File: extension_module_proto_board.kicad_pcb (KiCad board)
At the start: 2 copper layers, 32 parts, among them IC7 ATMEG328PU, P1 CONN_10, P10 CONN_40, P11 CONN_40, P12 CONN_40, P13 CONN_40, P14 CONN_40, P15 CONN_4, P16 CONN_6, P2 CONN_8, P3 CONN_6, P4 CONN_6, P5 CONN_40, P6 CONN_40, P7 CONN_40, P8 CONN_40, P9 CONN_40, SW1 DPST, U1 RBBB, X1 16MHz

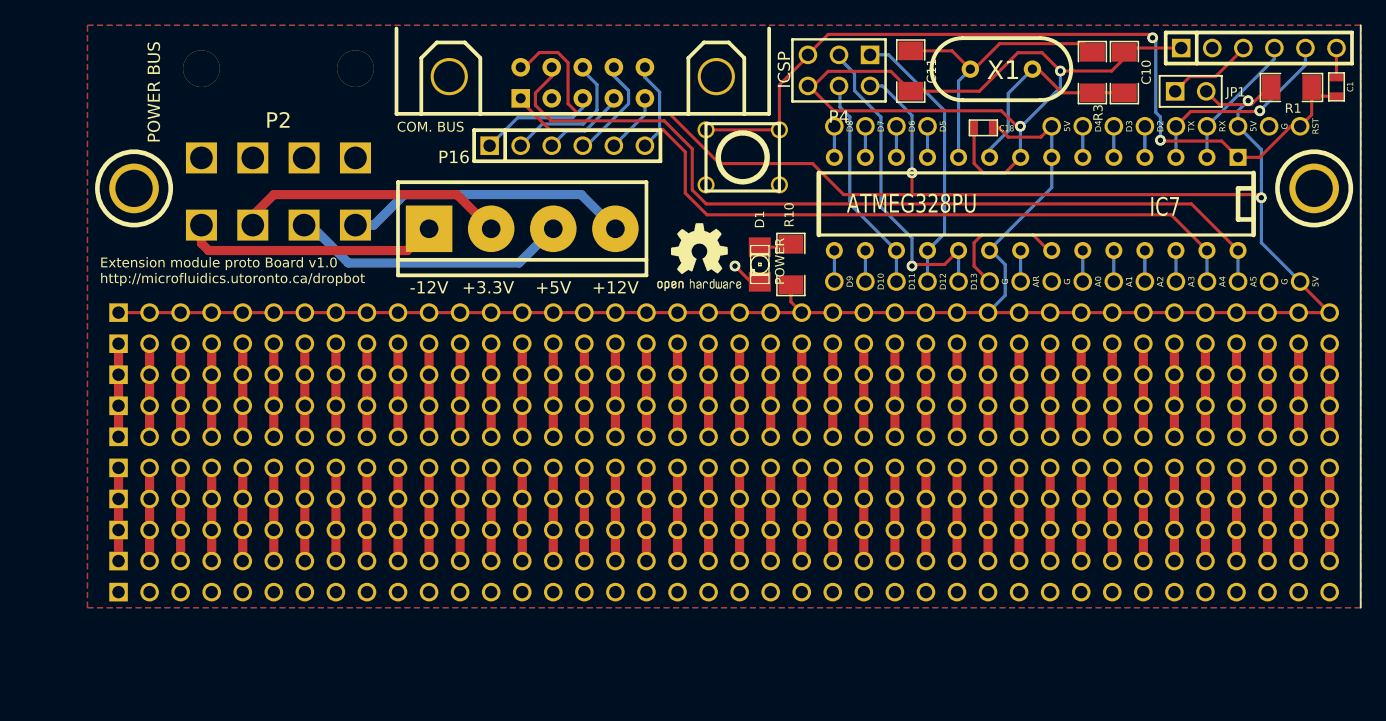
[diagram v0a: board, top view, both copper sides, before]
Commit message: Add ISP programming latch and other changes
* change layout to make board smaller
* replace 0603 caps with 1206 versions
* label VCC and GND rails
* add GND and VCC rail on either side of proto area
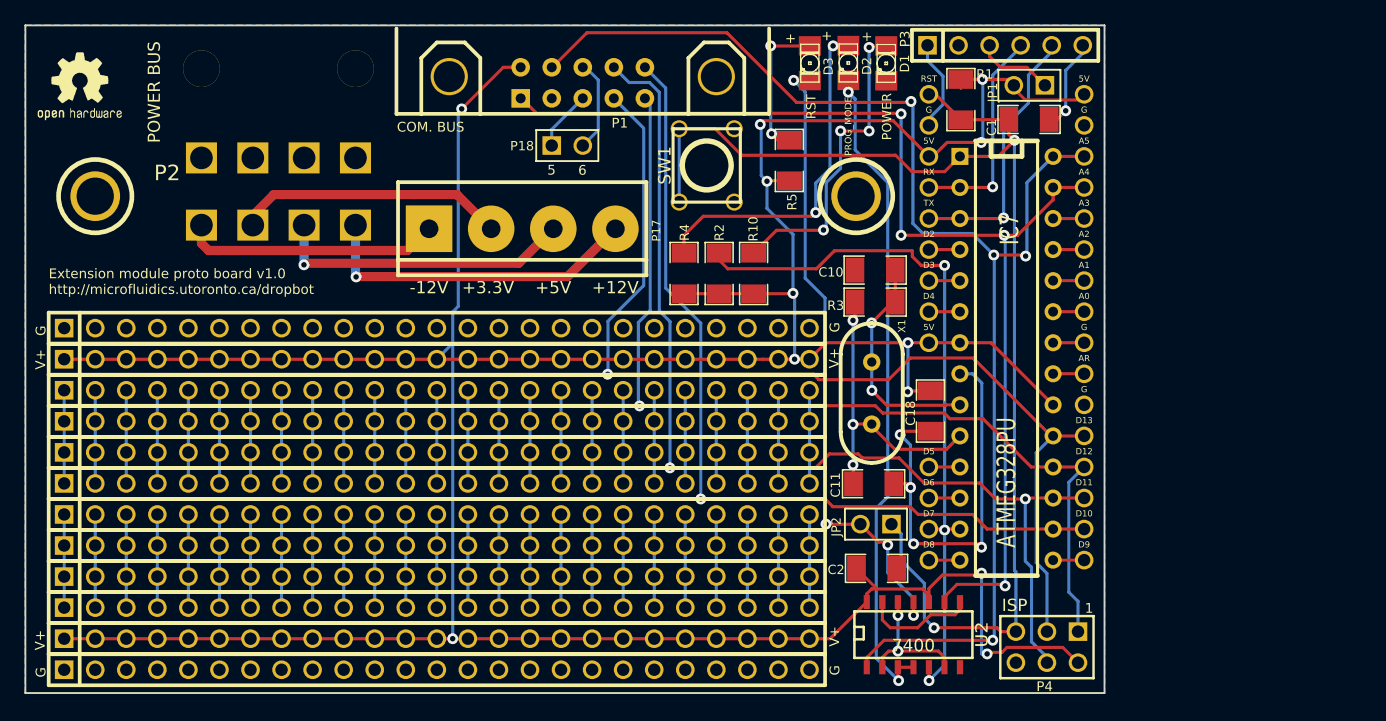
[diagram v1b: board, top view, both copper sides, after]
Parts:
- added C2: 0.1uF, SM1206, F.Cu at (84.9, 70.4)
- added D2: PROG_MODE, LED-1206, F.Cu at (82.5, 29.1)
- added D3: RST, LED-1206, F.Cu at (79.4, 29.1)
- added JP2: JUMPER, PIN_ARRAY_2X1, F.Cu at (84.8, 66.8)
- added P17: CONN_4, bornier4, F.Cu at (55.9, 42.7)
- added P18: CONN_2, PIN_ARRAY_2X1, F.Cu at (59.6, 35.9)
- added R2: 1k, SM1206, F.Cu at (72.0, 46.3)
- added R4: 1k, SM1206, F.Cu at (69.1, 46.3)
- added R5: 1k, SM1206, F.Cu at (77.7, 37.1)
- added U2: 7400, SO14E, F.Cu at (87.9, 75.7)
- C1, C18: footprint SM0603 -> SM1206
- P10, P11, P12, P13, P14, P5, P6, P7, P8, P9: value CONN_40 -> CONN_25; footprint PIN_ARRAY_40X1 -> PIN_ARRAY_25X1
- P15: value CONN_4 -> CONN_25; footprint bornier4 -> PIN_ARRAY_25X1
- P16: value CONN_6 -> CONN_25; footprint PIN_ARRAY-6X1 -> PIN_ARRAY_25X1
- R10: value 374 -> 1k
- moved G*** 52.6 mm to (15.9, 27.3)
- moved P4 50.1 mm to (98.8, 76.9)
- moved P16 44.5 mm to (47.6, 78.7)
- moved 1PIN 37.5 mm to (83.2, 40.0), turned to 90 degrees
- moved P5 34.7 mm to (47.6, 76.2)
- moved C11 33.9 mm to (84.6, 63.5), turned to 180 degrees
- moved X1 28.5 mm to (84.5, 56.1), turned to 90 degrees
- moved R1 27.1 mm to (91.8, 32.1), turned to 90 degrees
- moved C10 26.0 mm to (84.7, 46.1), turned to 0 degrees
- moved R3 25.8 mm to (84.7, 48.7), turned to 180 degrees
- moved C1 25.3 mm to (97.3, 33.7), turned to 180 degrees
- moved C18 23.6 mm to (89.3, 57.6), turned to 270 degrees
- moved P10 22.3 mm to (47.6, 63.5)
- moved P11 22.3 mm to (47.6, 66.0)
- moved P12 22.3 mm to (47.6, 68.6)
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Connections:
- P1 pad 10: N-0000047 -> D10
- P1 pad 5: N-0000051 -> N-000009
- P1 pad 6: N-0000050 -> N-000008
- P1 pad 7: N-0000049 -> D13/SCK
- P1 pad 8: N-0000045 -> D11/MOSI
- P1 pad 9: N-0000048 -> D12/MISO
- P10 pad 1: N-0000029 -> N-0000015
- P10 pad 10: N-0000015 -> N-0000023
- P10 pad 11: N-0000017 -> N-0000025
- P10 pad 12: N-0000014 -> N-0000027
- P10 pad 13: N-0000012 -> N-0000029
- P10 pad 14: N-000006 -> N-0000010
- P10 pad 15: N-000009 -> N-000003
- P10 pad 16: N-000007 -> N-000004
- P10 pad 17: N-000003 -> N-000005
- P10 pad 18: N-000002 -> N-000006
- P10 pad 19: N-000001 -> N-000007
- P10 pad 2: N-0000028 -> N-0000016
- P10 pad 20: N-000004 -> N-0000024
- P10 pad 21: N-000005 -> N-0000026
- P10 pad 22: N-0000013 -> N-0000028
- P10 pad 23: N-0000011 -> N-0000030
- P10 pad 24: N-0000010 -> N-0000013
- P10 pad 25: N-000008 -> N-0000014
- P10 pad 3: N-0000027 -> N-0000012
- P10 pad 4: N-0000026 -> N-0000017
- P10 pad 5: N-0000025 -> N-0000018
- P10 pad 6: N-0000024 -> N-0000019
- P10 pad 7: N-0000023 -> N-0000020
- P10 pad 9: N-0000020 -> N-0000022
- P11 pad 1: N-0000029 -> N-0000074
- P11 pad 10: N-0000015 -> N-0000083
- P11 pad 11: N-0000017 -> N-0000069
- P11 pad 12: N-0000014 -> N-0000071
- P11 pad 13: N-0000012 -> N-0000073
- P11 pad 14: N-000006 -> N-0000085
- P11 pad 15: N-000009 -> N-0000087
- P11 pad 16: N-000007 -> N-0000089
- P11 pad 17: N-000003 -> N-0000090
- P11 pad 18: N-000002 -> N-0000091
- P11 pad 19: N-000001 -> N-0000092
- P11 pad 2: N-0000028 -> N-0000075
- P11 pad 20: N-000004 -> N-0000068
- P11 pad 21: N-000005 -> N-0000070
- P11 pad 22: N-0000013 -> N-0000072
- P11 pad 23: N-0000011 -> N-0000084
- P11 pad 24: N-0000010 -> N-0000086
- P11 pad 25: N-000008 -> N-0000088
- P11 pad 3: N-0000027 -> N-0000076
- P11 pad 4: N-0000026 -> N-0000077
- P11 pad 5: N-0000025 -> N-0000078
- P11 pad 6: N-0000024 -> N-0000079
- P11 pad 7: N-0000023 -> N-0000080
- P11 pad 8: N-0000021 -> N-0000081
- P11 pad 9: N-0000020 -> N-0000082
- P12 pad 1: N-0000029 -> N-0000074
- P12 pad 10: N-0000015 -> N-0000083
- P12 pad 11: N-0000017 -> N-0000069
- P12 pad 12: N-0000014 -> N-0000071
- P12 pad 13: N-0000012 -> N-0000073
- P12 pad 14: N-000006 -> N-0000085
- P12 pad 15: N-000009 -> N-0000087
- P12 pad 16: N-000007 -> N-0000089
- P12 pad 17: N-000003 -> N-0000090
- P12 pad 18: N-000002 -> N-0000091
- P12 pad 19: N-000001 -> N-0000092
- P12 pad 2: N-0000028 -> N-0000075
- P12 pad 20: N-000004 -> N-0000068
- P12 pad 21: N-000005 -> N-0000070
- P12 pad 22: N-0000013 -> N-0000072
- P12 pad 23: N-0000011 -> N-0000084
- P12 pad 24: N-0000010 -> N-0000086
- P12 pad 25: N-000008 -> N-0000088
- P12 pad 3: N-0000027 -> N-0000076
- P12 pad 4: N-0000026 -> N-0000077
- P12 pad 5: N-0000025 -> N-0000078
- P12 pad 6: N-0000024 -> N-0000079
- P12 pad 7: N-0000023 -> N-0000080
- P12 pad 8: N-0000021 -> N-0000081
- P12 pad 9: N-0000020 -> N-0000082
- P13 pad 1: N-0000029 -> N-0000074
- P13 pad 10: N-0000015 -> N-0000083
- P13 pad 11: N-0000017 -> N-0000069
- P13 pad 12: N-0000014 -> N-0000071
- P13 pad 13: N-0000012 -> N-0000073
- P13 pad 14: N-000006 -> N-0000085
- P13 pad 15: N-000009 -> N-0000087
- P13 pad 16: N-000007 -> N-0000089
- P13 pad 17: N-000003 -> N-0000090
- P13 pad 18: N-000002 -> N-0000091
- P13 pad 19: N-000001 -> N-0000092
- P13 pad 2: N-0000028 -> N-0000075
- P13 pad 20: N-000004 -> N-0000068
- P13 pad 21: N-000005 -> N-0000070
- P13 pad 22: N-0000013 -> N-0000072
- P13 pad 23: N-0000011 -> N-0000084
- P13 pad 24: N-0000010 -> N-0000086
- P13 pad 25: N-000008 -> N-0000088
- P13 pad 3: N-0000027 -> N-0000076
- P13 pad 4: N-0000026 -> N-0000077
- P13 pad 5: N-0000025 -> N-0000078
- P13 pad 6: N-0000024 -> N-0000079
- P13 pad 7: N-0000023 -> N-0000080
- P13 pad 8: N-0000021 -> N-0000081
- P13 pad 9: N-0000020 -> N-0000082
- P14 pad 1: GND -> N-0000074
- P14 pad 10: GND -> N-0000083
- P14 pad 11: GND -> N-0000069
- P14 pad 12: GND -> N-0000071
- P14 pad 13: GND -> N-0000073
- P14 pad 14: GND -> N-0000085
- P14 pad 15: GND -> N-0000087
- P14 pad 16: GND -> N-0000089
- P14 pad 17: GND -> N-0000090
- P14 pad 18: GND -> N-0000091
- P14 pad 19: GND -> N-0000092
- P14 pad 2: GND -> N-0000075
- P14 pad 20: GND -> N-0000068
- P14 pad 21: GND -> N-0000070
- P14 pad 22: GND -> N-0000072
- P14 pad 23: GND -> N-0000084
- P14 pad 24: GND -> N-0000086
- P14 pad 25: GND -> N-0000088
- P14 pad 3: GND -> N-0000076
- P14 pad 4: GND -> N-0000077
- P14 pad 5: GND -> N-0000078
- P14 pad 6: GND -> N-0000079
- P14 pad 7: GND -> N-0000080
- P14 pad 8: GND -> N-0000081
- P14 pad 9: GND -> N-0000082
- P15 pad 1: -12V PWR -> GND
- P15 pad 2: +3.3V PWR -> GND
- P15 pad 3: +5V PWR -> GND
- P15 pad 4: +12V PWR -> GND
- P16 pad 1: N-0000051 -> GND
- P16 pad 2: N-0000050 -> GND
- P16 pad 3: N-0000049 -> GND
- P16 pad 4: N-0000045 -> GND
- P16 pad 5: N-0000048 -> GND
- P16 pad 6: N-0000047 -> GND
- P6 pad 1: N-00000120 -> VCC
- P6 pad 10: N-00000112 -> VCC
- P6 pad 11: N-00000108 -> VCC
- P6 pad 12: N-0000097 -> VCC
- P6 pad 13: N-0000094 -> VCC
- P6 pad 14: N-0000091 -> VCC
- P6 pad 15: N-0000088 -> VCC
- P6 pad 16: N-0000085 -> VCC
- P6 pad 17: N-0000082 -> VCC
- P6 pad 18: N-00000105 -> VCC
- P6 pad 19: N-00000102 -> VCC
- P6 pad 2: N-00000119 -> VCC
- P6 pad 20: N-00000111 -> VCC
- P6 pad 21: N-0000099 -> VCC
- P6 pad 22: N-0000096 -> VCC
- P6 pad 23: N-0000093 -> VCC
- P6 pad 24: N-0000081 -> VCC
- P6 pad 25: N-0000087 -> VCC
- P6 pad 3: N-00000118 -> VCC
- P6 pad 4: N-00000117 -> VCC
- P6 pad 5: N-00000116 -> VCC
- P6 pad 6: N-00000107 -> VCC
- P6 pad 7: N-00000115 -> VCC
- P6 pad 8: N-00000114 -> VCC
- P6 pad 9: N-00000113 -> VCC
- P7 pad 1: N-00000120 -> N-0000015
- P7 pad 10: N-00000112 -> N-0000023
- P7 pad 11: N-00000108 -> N-0000025
- P7 pad 12: N-0000097 -> N-0000027
- P7 pad 13: N-0000094 -> N-0000029
- P7 pad 14: N-0000091 -> N-0000010
- P7 pad 15: N-0000088 -> N-000003
- P7 pad 16: N-0000085 -> N-000004
- P7 pad 17: N-0000082 -> N-000005
- P7 pad 18: N-00000105 -> N-000006
- P7 pad 19: N-00000102 -> N-000007
- P7 pad 2: N-00000119 -> N-0000016
- P7 pad 20: N-00000111 -> N-0000024
- P7 pad 21: N-0000099 -> N-0000026
- P7 pad 22: N-0000096 -> N-0000028
- P7 pad 23: N-0000093 -> N-0000030
- P7 pad 24: N-0000081 -> N-0000013
- P7 pad 25: N-0000087 -> N-0000014
- P7 pad 3: N-00000118 -> N-0000012
- P7 pad 4: N-00000117 -> N-0000017
- P7 pad 5: N-00000116 -> N-0000018
- P7 pad 6: N-00000107 -> N-0000019
- P7 pad 7: N-00000115 -> N-0000020
- P7 pad 8: N-00000114 -> N-0000021
- P7 pad 9: N-00000113 -> N-0000022
- P8 pad 1: N-00000120 -> N-0000015
- P8 pad 10: N-00000112 -> N-0000023
- P8 pad 11: N-00000108 -> N-0000025
- P8 pad 12: N-0000097 -> N-0000027
- P8 pad 13: N-0000094 -> N-0000029
- P8 pad 14: N-0000091 -> N-0000010
- P8 pad 15: N-0000088 -> N-000003
- P8 pad 16: N-0000085 -> N-000004
- P8 pad 17: N-0000082 -> N-000005
- P8 pad 18: N-00000105 -> N-000006
- P8 pad 19: N-00000102 -> N-000007
- P8 pad 2: N-00000119 -> N-0000016
- P8 pad 20: N-00000111 -> N-0000024
- P8 pad 21: N-0000099 -> N-0000026
- P8 pad 22: N-0000096 -> N-0000028
- P8 pad 23: N-0000093 -> N-0000030
- P8 pad 24: N-0000081 -> N-0000013
- P8 pad 25: N-0000087 -> N-0000014
- P8 pad 3: N-00000118 -> N-0000012
- P8 pad 4: N-00000117 -> N-0000017
- P8 pad 5: N-00000116 -> N-0000018
- P8 pad 6: N-00000107 -> N-0000019
- P8 pad 7: N-00000115 -> N-0000020
- P8 pad 8: N-00000114 -> N-0000021
- P8 pad 9: N-00000113 -> N-0000022
- P9 pad 1: N-00000120 -> N-0000015
- P9 pad 10: N-00000112 -> N-0000023
- P9 pad 11: N-00000108 -> N-0000025
- P9 pad 12: N-0000097 -> N-0000027
- P9 pad 13: N-0000094 -> N-0000029
- P9 pad 14: N-0000091 -> N-0000010
- P9 pad 15: N-0000088 -> N-000003
- P9 pad 16: N-0000085 -> N-000004
- P9 pad 17: N-0000082 -> N-000005
- P9 pad 18: N-00000105 -> N-000006
- P9 pad 19: N-00000102 -> N-000007
- P9 pad 2: N-00000119 -> N-0000016
- P9 pad 20: N-00000111 -> N-0000024
- P9 pad 21: N-0000099 -> N-0000026
- P9 pad 22: N-0000096 -> N-0000028
- P9 pad 23: N-0000093 -> N-0000030
- P9 pad 24: N-0000081 -> N-0000013
- P9 pad 25: N-0000087 -> N-0000014
- P9 pad 3: N-00000118 -> N-0000012
- P9 pad 4: N-00000117 -> N-0000017
- P9 pad 5: N-00000116 -> N-0000018
- P9 pad 6: N-00000107 -> N-0000019
- P9 pad 7: N-00000115 -> N-0000020
- P9 pad 8: N-00000114 -> N-0000021
- P9 pad 9: N-00000113 -> N-0000022
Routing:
- net VCC: track 233.4 -> 306.7 mm, vias 3 -> 12
- net D11/MOSI: track 17.9 -> 85.7 mm, vias 0 -> 2
- net D10: track 2.54 -> 69.6 mm, vias 0 -> 1
- net D13/SCK: track 27.0 -> 84.3 mm
- net D7: track 2.54 -> 58.9 mm, vias 0 -> 3
- net D12/MISO: track 22.6 -> 78.5 mm, vias 0 -> 1
- net N-0000052: track 0.00 -> 52.2 mm, vias 0 -> 4
- net N-000002: track 7.62 -> 54.0 mm, vias 0 -> 2
- net GND: track 82.7 -> 44.8 mm, vias 3 -> 4
- net A5/SCL: track 70.6 -> 108.2 mm, vias 0 -> 4
- net RST: track 70.5 -> 102.2 mm
- net N-0000067: track 0.00 -> 28.5 mm, vias 0 -> 2
- net A4/SDA: track 65.9 -> 93.3 mm, vias 0 -> 4
- net N-0000066: track 2.64 -> 25.9 mm, vias 0 -> 4
- net N-0000053: track 0.00 -> 12.1 mm, vias 0 -> 2
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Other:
- board outline added: 88.3 x 54.6 mm
- board text added: "+"
- board text added: "1"
- board text added: "5"
- board text added: "6"
- board text added: "Extension module proto board v1.0 http://microfluidics.utoronto.ca/dropbot"
- board text added: "G"
- board text added: "ISP"
- board text added: "V+"
- board text removed: "Extension module proto Board v1.0 http://microfluidics.utoronto.ca/dropbot"
- board text removed: "ICSP"

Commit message: Fix BOM and labels
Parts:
- JP2: value JUMPER -> ISP RESET
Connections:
- net D7 renamed D7/ISP_ENABLE
